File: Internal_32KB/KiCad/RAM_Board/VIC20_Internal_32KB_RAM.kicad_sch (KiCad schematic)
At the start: 12 parts, among them J1 UD4, J2 UE4, J3 Switch, J4 RAM Decode, J5 BLK Inputs, J6 BLK Outputs, U1 62256, U2 RAM Decoder, U3 BLK Decoder

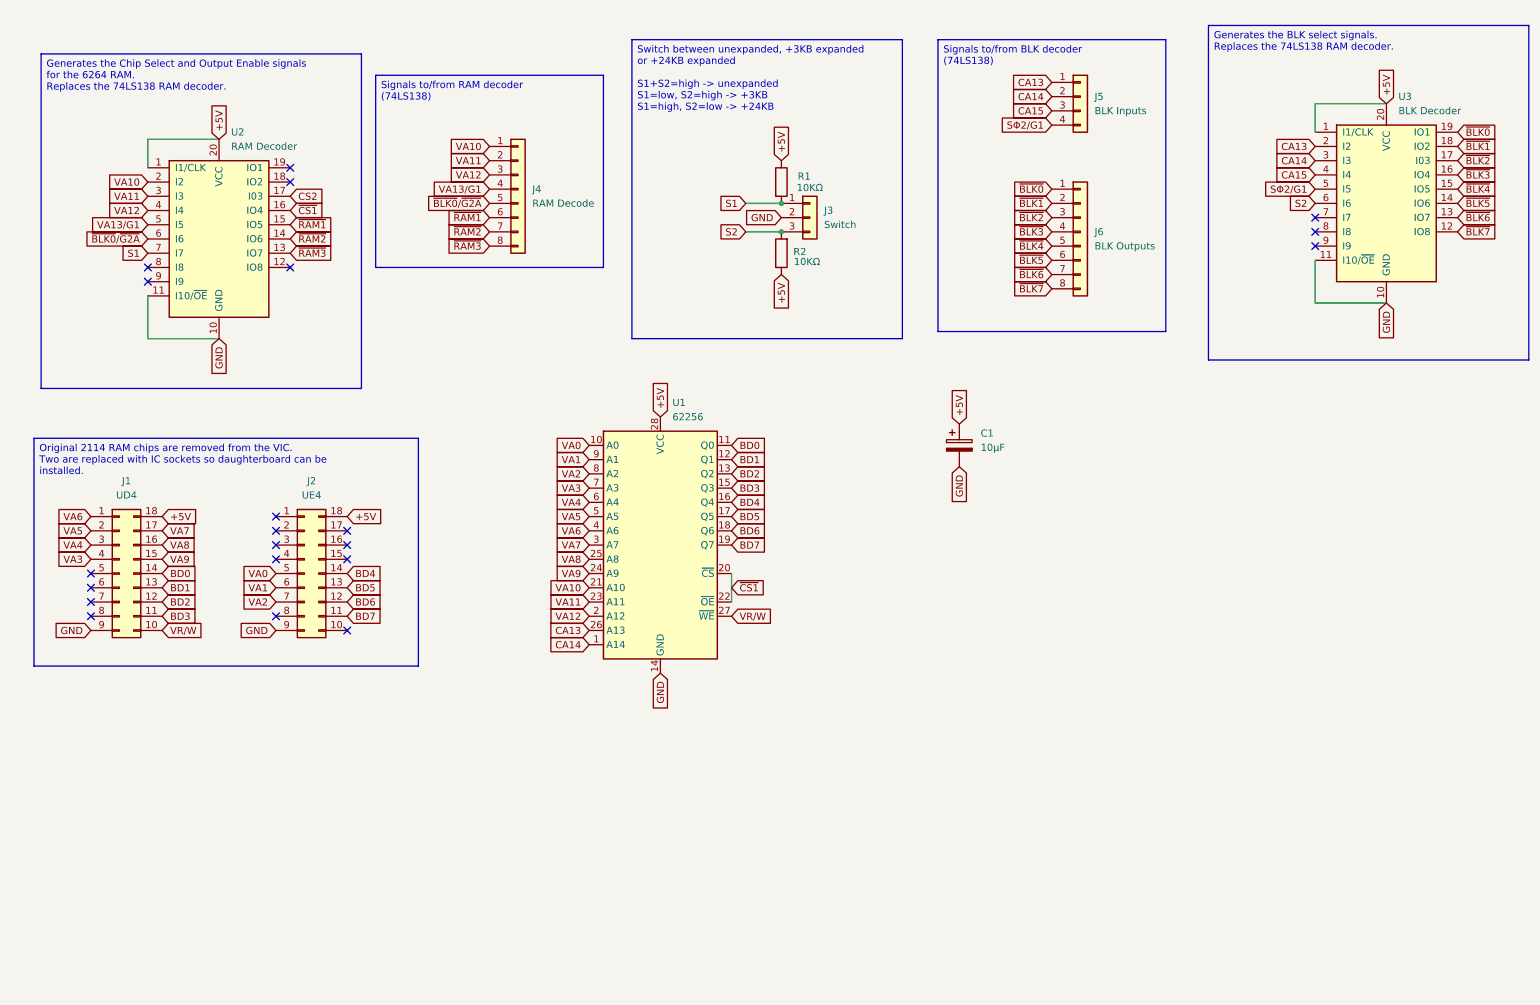
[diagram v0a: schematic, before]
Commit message: Redesigned 32KB expansion
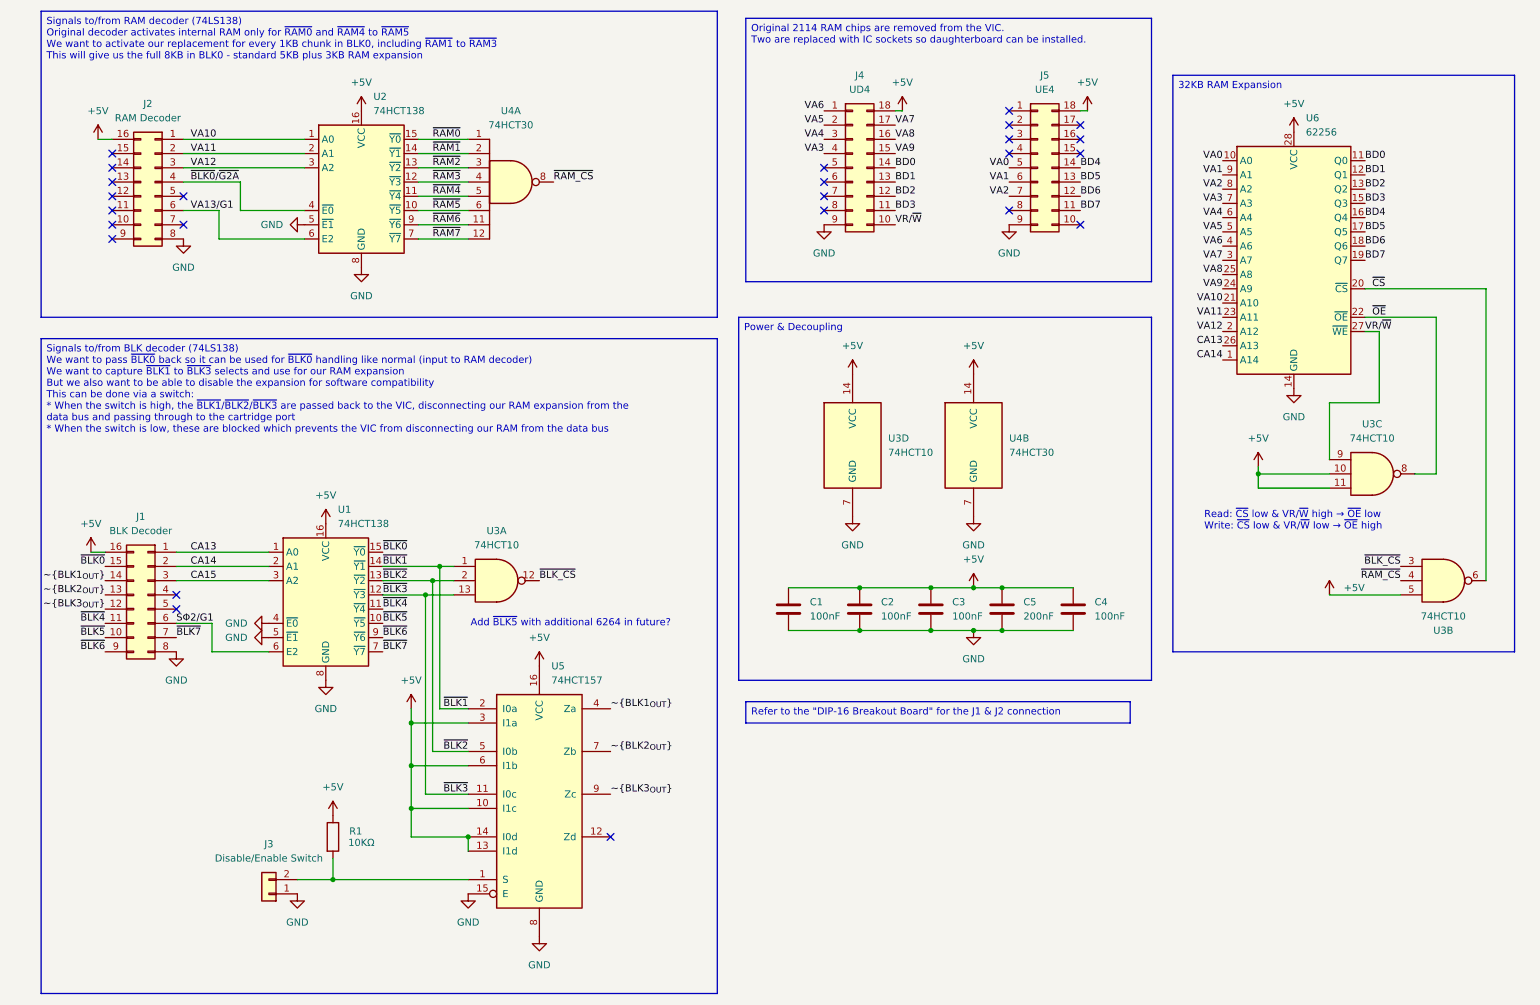
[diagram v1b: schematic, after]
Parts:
- removed C1: 10µF, Capacitor_THT:CP_Radial_D5.0mm_P2.50mm, symbol Device:C_Polarized
- removed J3: Switch, Connector_PinHeader_2.54mm:PinHeader_1x03_P2.54mm_Vertical, symbol Connector_Generic:Conn_01x03
- removed J4: RAM Decode, Connector_PinHeader_2.54mm:PinHeader_1x08_P2.54mm_Vertical, symbol Connector_Generic:Conn_01x08
- removed J5: BLK Inputs, Connector_PinHeader_2.54mm:PinHeader_1x04_P2.54mm_Vertical, symbol Connector_Generic:Conn_01x04
- removed J6: BLK Outputs, Connector_PinHeader_2.54mm:PinHeader_1x08_P2.54mm_Vertical, symbol Connector_Generic:Conn_01x08
- removed R2: 10KΩ, Resistor_THT:R_Axial_DIN0207_L6.3mm_D2.5mm_P7.62mm_Horizontal, symbol Device:R
- removed U2: RAM Decoder, Package_DIP:DIP-20_W7.62mm, symbol Logic_Programmable:GAL16V8
- removed U3: BLK Decoder, Package_DIP:DIP-20_W7.62mm, symbol Logic_Programmable:GAL16V8
- added C1, C2, C3, C4: 100nF, Capacitor_THT:C_Disc_D3.0mm_W2.0mm_P2.50mm, symbol Device:C
- added C5: 200nF, Capacitor_THT:C_Disc_D3.0mm_W2.0mm_P2.50mm, symbol Device:C
- added J1: BLK Decoder, Connector_PinHeader_2.54mm:PinHeader_2x08_P2.54mm_Vertical, symbol Connector_Generic:Conn_02x08_Counter_Clockwise
- added J2: RAM Decoder, Connector_PinHeader_2.54mm:PinHeader_2x08_P2.54mm_Vertical, symbol Connector_Generic:Conn_02x08_Counter_Clockwise
- added J3: Disable/Enable Switch, Connector_PinHeader_2.54mm:PinHeader_1x02_P2.54mm_Vertical, symbol Connector_Generic:Conn_01x02
- added U1, U2: 74HCT138, Package_DIP:DIP-16_W7.62mm, symbol 74xx:74HCT138
- added U3: 74HCT10, Package_DIP:DIP-14_W7.62mm, symbol 74xx:74LS10
- added U4: 74HCT30, Package_DIP:DIP-14_W7.62mm, symbol 74xx:74LS30
- added U5: 74HCT157, Package_DIP:DIP-16_W7.62mm, symbol 74xx:74LS157
- renumbered J1 to J4, J2 to J5, U1 to U6
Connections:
- net +5V: now also C1.1, C2.1, C3.1, C4.1, C5.1, J1.16 (Pin_16), J2.16 (Pin_16), U1.16 (VCC), U2.16 (VCC), U3.10, U3.11, U3.14 (VCC), U3.5, U4.14 (VCC), U5.10 (I1c), U5.13 (I1d), U5.14 (I0d), U5.16 (VCC), U5.3 (I1a), U5.6 (I1b)
- net CA13: now also J1.1 (Pin_1), U1.1 (A0)
- net CA14: now also J1.2 (Pin_2), U1.2 (A1)
- net CA15: now also J1.3 (Pin_3), U1.3 (A2)
- net GND: now also C1.2, C2.2, C3.2, C4.2, C5.2, J1.8 (Pin_8), J2.8 (Pin_8), J3.1 (Pin_1), U1.4 (~{E0}), U1.5 (~{E1}), U1.8 (GND), U2.5 (~{E1}), U2.8 (GND), U3.7 (GND), U4.7 (GND), U5.15 (E), U5.8 (GND)
- net SΦ2/G1: now also J1.6 (Pin_6), U1.6 (E2)
- net VA10: now also J2.1 (Pin_1), U2.1 (A0)
- net VA11: now also J2.2 (Pin_2), U2.2 (A1)
- net VA12: now also J2.3 (Pin_3), U2.3 (A2)
- net VA13/G1: now also J2.6 (Pin_6), U2.6 (E2)
- net ~{BLK0}: now also J1.15 (Pin_15), U1.15 (~{Y0})
- net ~{BLK0}/~{G2A}: now also J2.4 (Pin_4), U2.4 (~{E0})
- net ~{BLK1}: now also U1.14 (~{Y1}), U3.1, U5.2 (I0a)
- net ~{BLK2}: now also U1.13 (~{Y2}), U3.2, U5.5 (I0b)
- net ~{BLK3}: now also U1.12 (~{Y3}), U3.13, U5.11 (I0c)
- net ~{BLK4}: now also J1.11 (Pin_11), U1.11 (~{Y4})
- net ~{BLK5}: now also J1.10 (Pin_10), U1.10 (~{Y5})
- net ~{BLK6}: now also J1.9 (Pin_9), U1.9 (~{Y6})
- net ~{BLK7}: now also J1.7 (Pin_7), U1.7 (~{Y7})
- net ~{RAM1}: now also U2.14 (~{Y1}), U4.2
- net ~{RAM2}: now also U2.13 (~{Y2}), U4.3
- net ~{RAM3}: now also U2.12 (~{Y3}), U4.4
- net S1: no longer names the net of R1.2
- net S1: now also J3.2 (Pin_2), U5.1 (S)
- net VR/W renamed VR/~{W}
- net VR/~{W}: now also U3.9
- net ~{CS1} renamed ~{CS}
- net ~{CS}: now also U3.6; no longer U6.22 (~{OE})
- new net ~{BLK1_{OUT}}: J1.14 (Pin_14), U5.4 (Za)
- new net ~{BLK2_{OUT}}: J1.13 (Pin_13), U5.7 (Zb)
- new net ~{BLK3_{OUT}}: J1.12 (Pin_12), U5.9 (Zc)
- new net ~{BLK_CS}: U3.12, U3.3
- new net ~{OE}: U3.8, U6.22 (~{OE})
- new net ~{RAM0}: U2.15 (~{Y0}), U4.1
- new net ~{RAM4}: U2.11 (~{Y4}), U4.5
- new net ~{RAM5}: U2.10 (~{Y5}), U4.6
- new net ~{RAM6}: U2.9 (~{Y6}), U4.11
- new net ~{RAM7}: U2.7 (~{Y7}), U4.12
- new net ~{RAM_CS}: U3.4, U4.8
- no-connect marks 21 -> 25
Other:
- note added: "Add ~{BLK5} with additional 6264 in future?"
- note added: "Read: ~{CS} low & VR/~{W} high → ~{OE} low Write: ~{CS} low & VR/~{W} low → ~{OE} high"
- moved on the sheet: J4, J5, U6
